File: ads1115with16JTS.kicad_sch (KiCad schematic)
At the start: 52 parts, among them J1 Conn_01x02_Pin, J10 Conn_01x02_Pin, J11 Conn_01x02_Pin, J12 Conn_01x02_Pin, J13 Conn_01x02_Pin, J14 Conn_01x02_Pin, J15 Conn_01x02_Pin, J16 Conn_01x02_Pin, J17 Conn_01x04_Pin, J18 PinSocket_1x20_P2.54mm_Vertic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, J19 PinSocket_1x20_P2.54mm_Vertic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, J2 Conn_01x02_Pin, J20 Screw_Terminal_01x02, J3 Conn_01x02_Pin, J4 Conn_01x02_Pin, J5 Conn_01x02_Pin, J6 Conn_01x02_Pin, J7 Conn_01x02_Pin, J8 Conn_01x02_Pin, J9 Conn_01x02_Pin, U1 ADS1115IDGS, U2 ADS1115IDGS, U3 ADS1115IDGS, U4 ADS1115IDGS

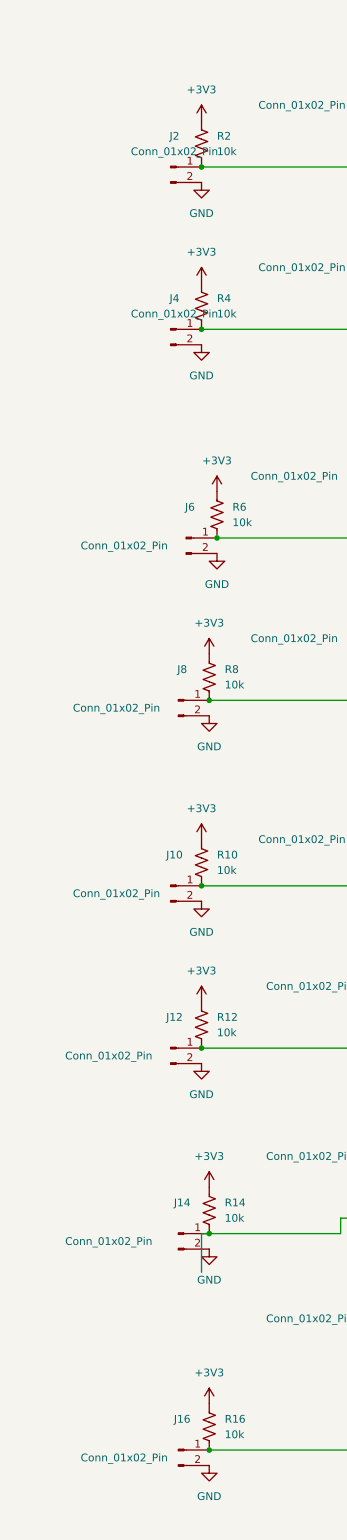
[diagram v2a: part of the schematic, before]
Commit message: sized slightly larger, added 2 more mounting holes.
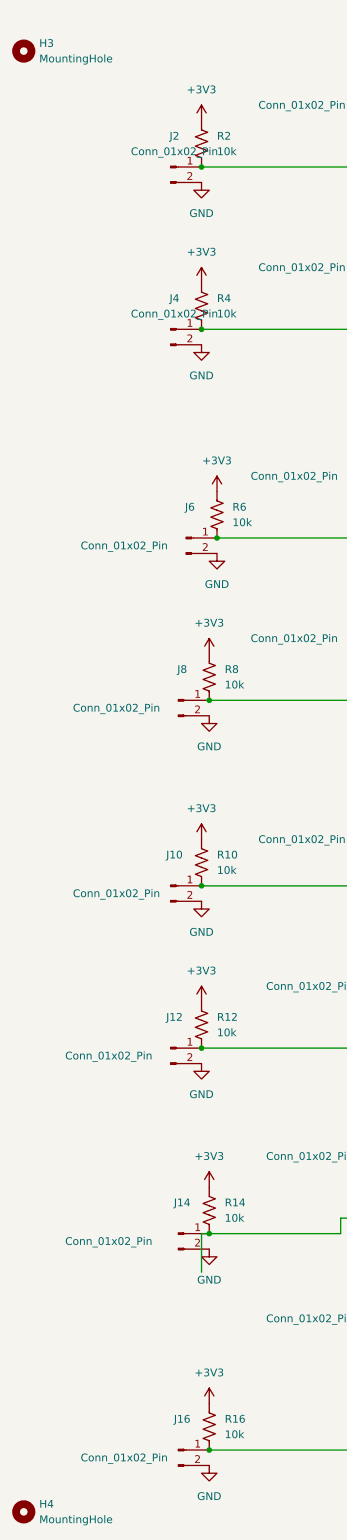
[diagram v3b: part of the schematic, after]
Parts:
- added H3, H4: MountingHole, MountingHole:MountingHole_2.2mm_M2_ISO7380_Pad, symbol ProjectLib:MountingHole
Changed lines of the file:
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@@
+    )
+  )
+  (symbol (lib_id "ProjectLib:MountingHole") (at 19.05 20.32 0) (unit 1)
+    (in_bom yes) (on_board yes) (dnp no) (fields_autoplaced)
+    (property "Reference" "H3" (at 21.59 19.05 0)
+      (effects (font (size 1.27 1.27)) (justify left))
+    )
+    (property "Value" "MountingHole" (at 21.59 21.59 0)
+      (effects (font (size 1.27 1.27)) (justify left))
+    )
+    (property "Footprint" "MountingHole:MountingHole_2.2mm_M2_ISO7380_Pad" (at 19.05 20.32 0)
+      (effects (font (size 1.27 1.27)) hide)
+    )
+    (property "Datasheet" "~" (at 19.05 20.32 0)
+      (effects (font (size 1.27 1.27)) hide)
+    )
+    (instances
+      (project "ads1115with16JTS"
+        (path "/0c2d0c14-8850-4a30-bb78-b2f40cb442ba"
+          (reference "H3") (unit 1)
+        )
+      )
     )
   )
@@
         )
       )
+    )
+  )
+  (symbol (lib_id "ProjectLib:MountingHole") (at 19.05 260.35 0) (unit 1)
+    (in_bom yes) (on_board yes) (dnp no) (fields_autoplaced)
+    (property "Reference" "H4" (at 21.59 259.08 0)
+      (effects (font (size 1.27 1.27)) (justify left))
+    )
+    (property "Value" "MountingHole" (at 21.59 261.62 0)
+      (effects (font (size 1.27 1.27)) (justify left))
+    )
+    (property "Footprint" "MountingHole:MountingHole_2.2mm_M2_ISO7380_Pad" (at 19.05 260.35 0)
+      (effects (font (size 1.27 1.27)) hide)
+    )
+    (property "Datasheet" "~" (at 19.05 260.35 0)
+      (effects (font (size 1.27 1.27)) hide)
+    )
+    (instances
+      (project "ads1115with16JTS"
+        (path "/0c2d0c14-8850-4a30-bb78-b2f40cb442ba"
+          (reference "H4") (unit 1)
+        )
+      )

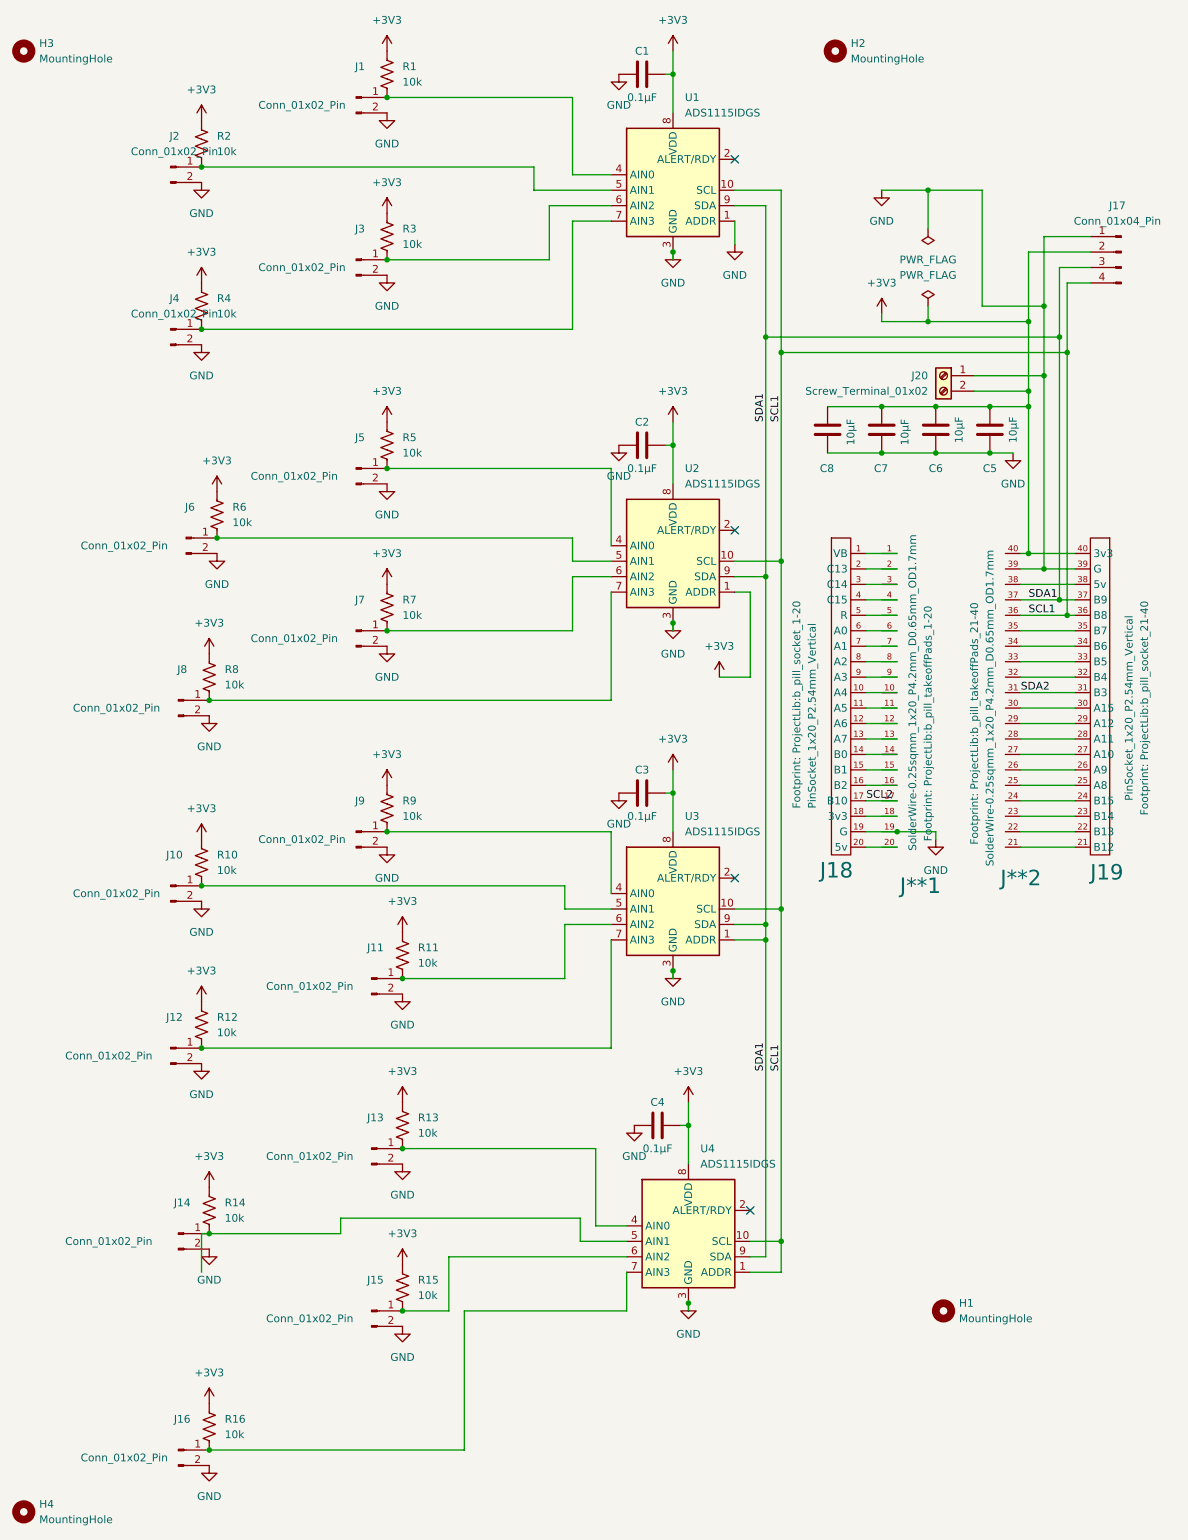
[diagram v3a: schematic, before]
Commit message: Footprint adjustments to get tthem all from ProjectLib.pretty. Using Kicad 8.0.1.
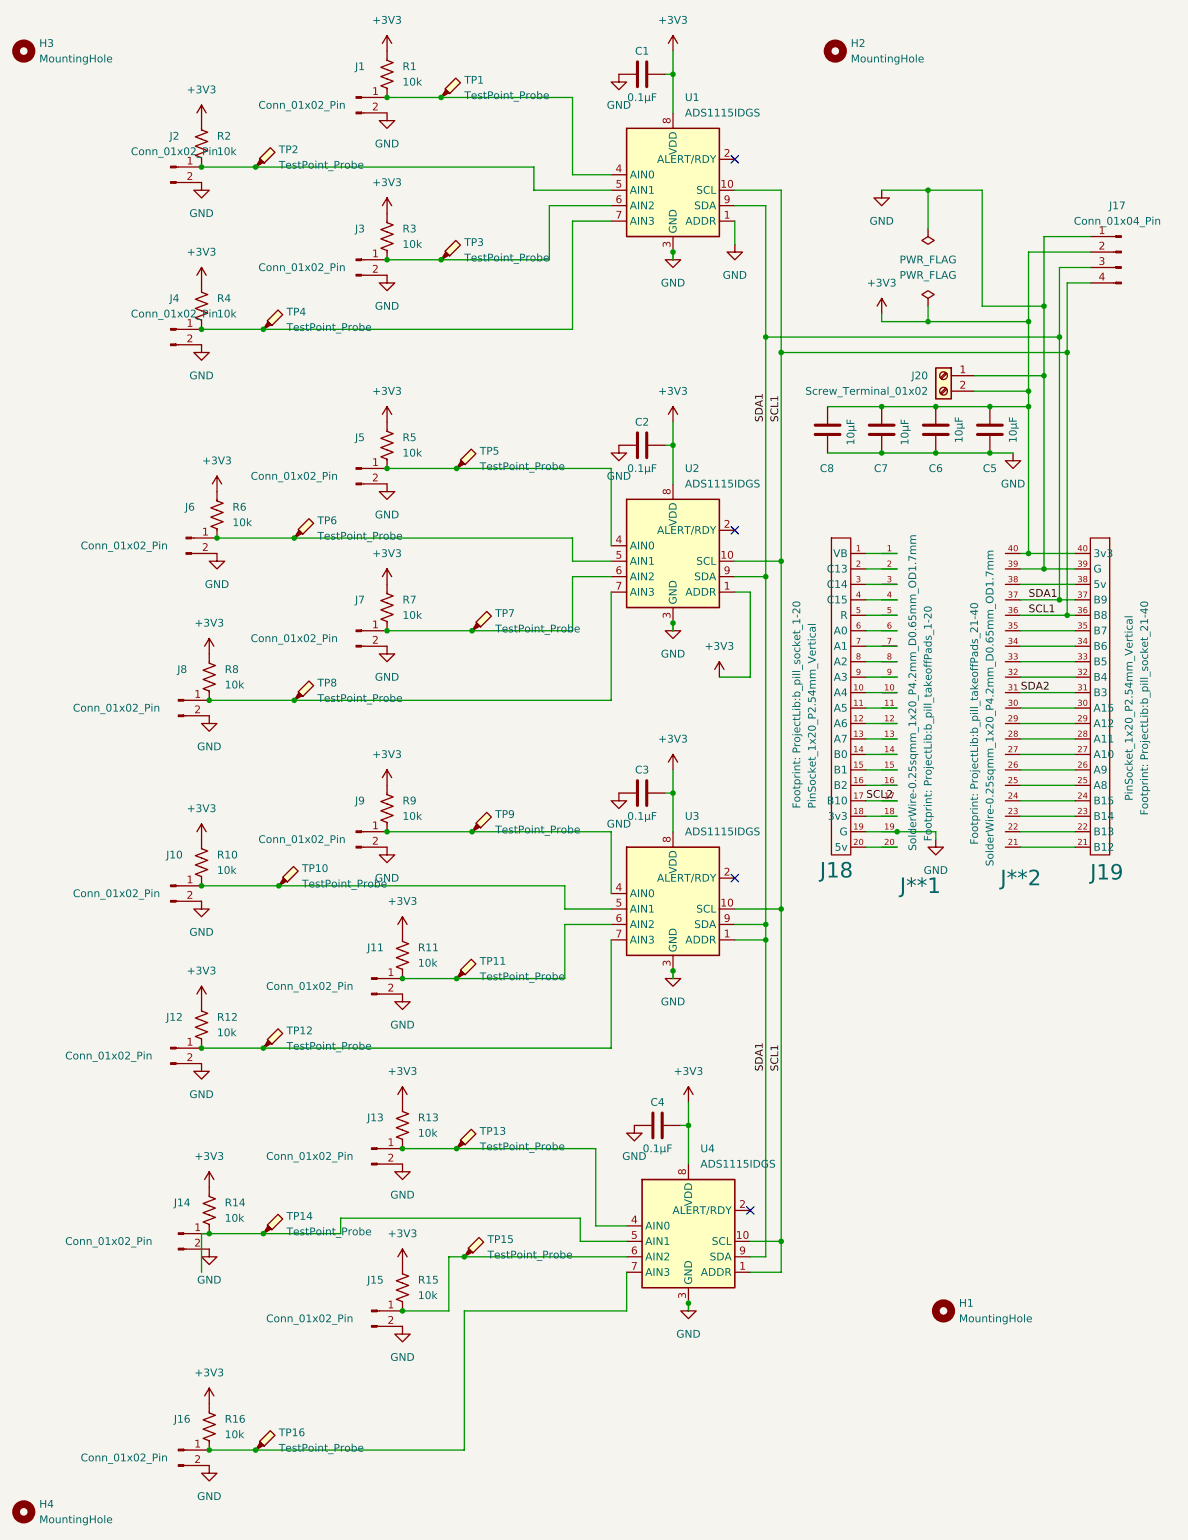
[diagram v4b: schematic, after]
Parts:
- added TP1, TP10, TP11, TP12, TP13, TP14, TP15, TP16, TP2, TP3, TP4, TP5, TP6, TP7, TP8, TP9: TestPoint_Probe, TestPoint:TestPoint_THTPad_D1.0mm_Drill0.5mm, symbol ProjectLib:TestPoint_Probe
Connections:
- net at J15.1 (Pin_1), R15.2, U4.6 (AIN2): now also TP15.1
- net at J1.1 (Pin_1), R1.2, U1.4 (AIN0): now also TP1.1
- net at J2.1 (Pin_1), R2.2, U1.5 (AIN1): now also TP2.1
- net at J3.1 (Pin_1), R3.2, U1.6 (AIN2): now also TP3.1
- net at J4.1 (Pin_1), R4.2, U1.7 (AIN3): now also TP4.1
- net at J16.1 (Pin_1), R16.2, U4.7 (AIN3): now also TP16.1
- net at J12.1 (Pin_1), R12.2, U3.7 (AIN3): now also TP12.1
- net at J11.1 (Pin_1), R11.2, U3.6 (AIN2): now also TP11.1
- net at J13.1 (Pin_1), R13.2, U4.4 (AIN0): now also TP13.1
- net at J14.1 (Pin_1), R14.2, U4.5 (AIN1): now also TP14.1
- net at J10.1 (Pin_1), R10.2, U3.5 (AIN1): now also TP10.1
- net at J8.1 (Pin_1), R8.2, U2.7 (AIN3): now also TP8.1
- net at J9.1 (Pin_1), R9.2, U3.4 (AIN0): now also TP9.1
- net at J7.1 (Pin_1), R7.2, U2.6 (AIN2): now also TP7.1
- net at J6.1 (Pin_1), R6.2, U2.5 (AIN1): now also TP6.1
- net at J5.1 (Pin_1), R5.2, U2.4 (AIN0): now also TP5.1

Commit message: Removed test points because there is no room. Trying to sync symbol footprints and pcb footprints.
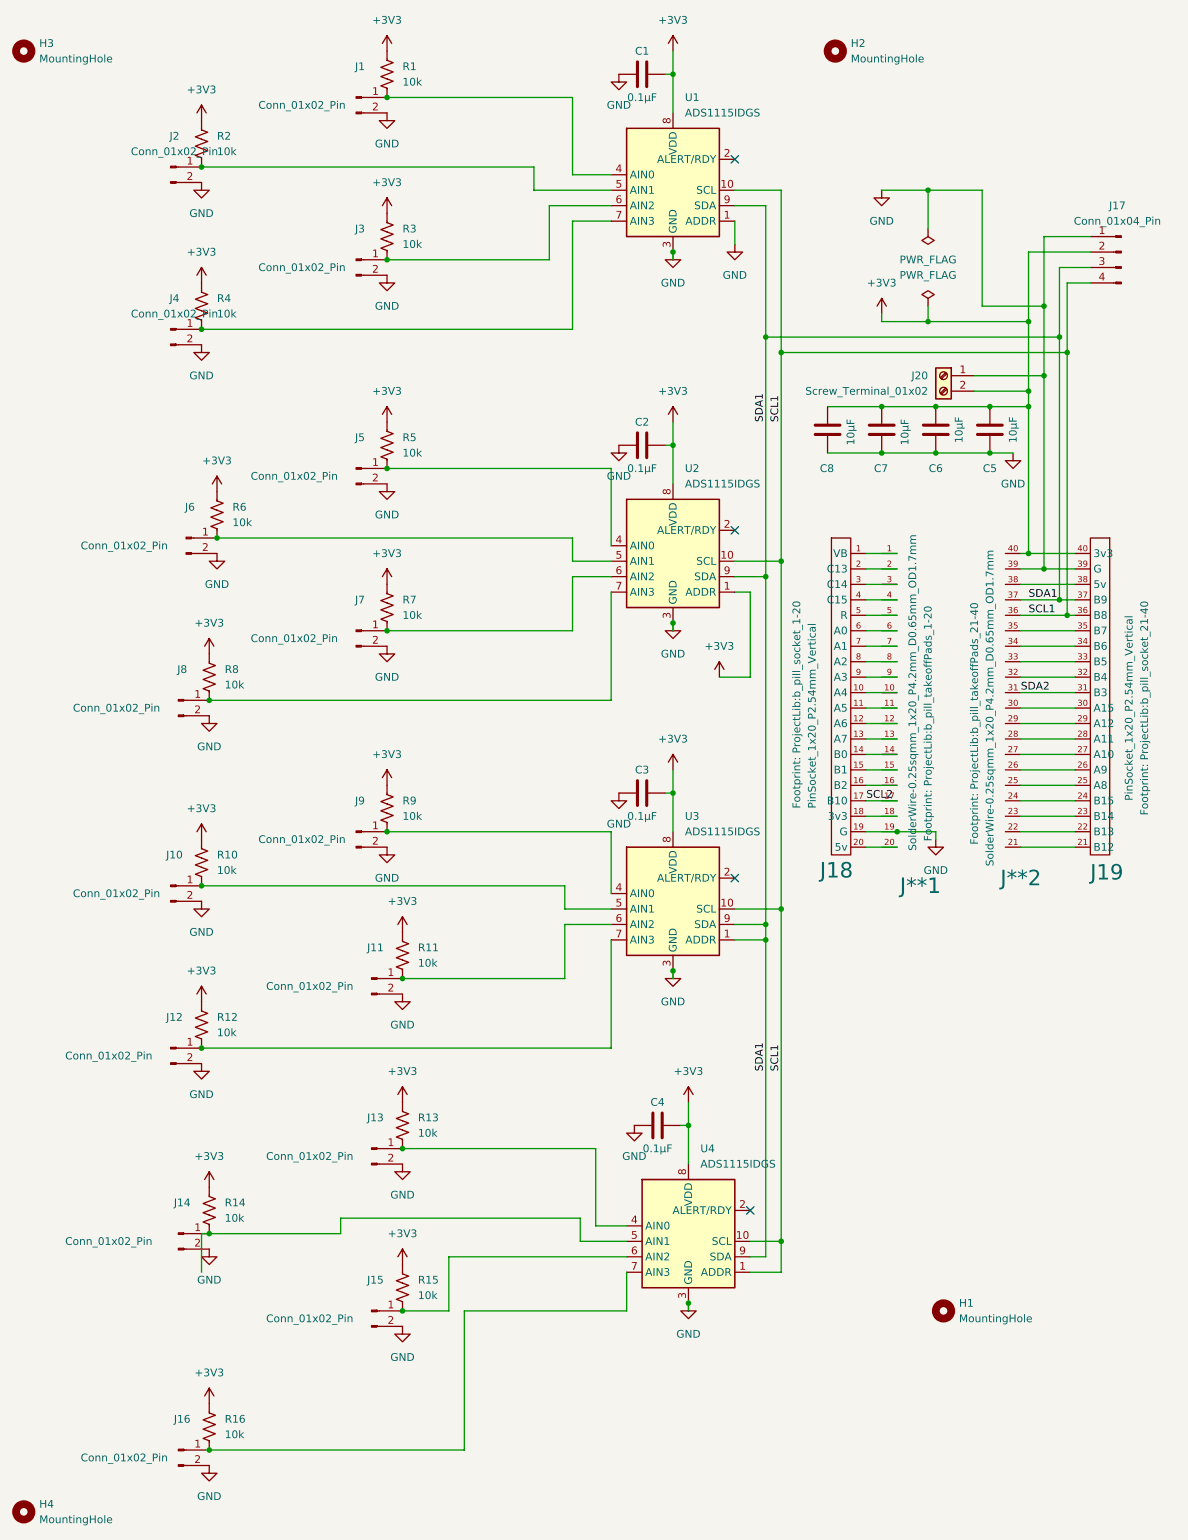
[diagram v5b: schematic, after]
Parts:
- removed TP1, TP10, TP11, TP12, TP13, TP14, TP15, TP16, TP2, TP3, TP4, TP5, TP6, TP7, TP8, TP9: TestPoint_Probe, TestPoint:TestPoint_THTPad_D1.0mm_Drill0.5mm, symbol ProjectLib:TestPoint_Probe
- H1, H2, H3, H4: footprint MountingHole:MountingHole_2.2mm_M2_ISO7380_Pad -> ProjectLib:MountingHole_2.2mm_M2_ISO7380_Pad

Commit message: DRC runs clean.
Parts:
- removed C7, C8: 10µF, ProjectLib:C_0805_2012Metric, symbol Device:C
- added C7, C8: 10µF, ProjectLib:C_0805_2012Metric, symbol ProjectLib:C
- C1, C2, C3, C4, C5, C6: footprint Capacitor_SMD:C_0805_2012Metric -> ProjectLib:C_0805_2012Metric
- J1, J10, J11, J12, J13, J14, J15, J16, J2, J3, J4, J5, J6, J7, J8, J9: footprint Connector_JST:JST_XH_B2B-XH-A_1x02_P2.50mm_Vertical -> ProjectLib:JST_XH_B2B-XH-A_1x02_P2.50mm_Vertical
- J20: footprint TerminalBlock_Phoenix:TerminalBlock_Phoenix_MPT-0,5-2-2.54_1x02_P2.54mm_Horizontal -> ProjectLib:TerminalBlock_Phoenix_MPT-0,5-2-2.54_1x02_P2.54mm_Horizontal
- R1, R10, R11, R12, R13, R14, R15, R16, R2, R3, R4, R5, R6, R7, R8, R9: footprint Resistor_SMD:R_0603_1608Metric -> ProjectLib:R_0603_1608Metric
- U1, U2, U3, U4: footprint Package_SO:TSSOP-10_3x3mm_P0.5mm -> ProjectLib:TSSOP-10_3x3mm_P0.5mm
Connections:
- net +3V3: now also C7.1, C8.1
- net GND: now also C7.2, C8.2

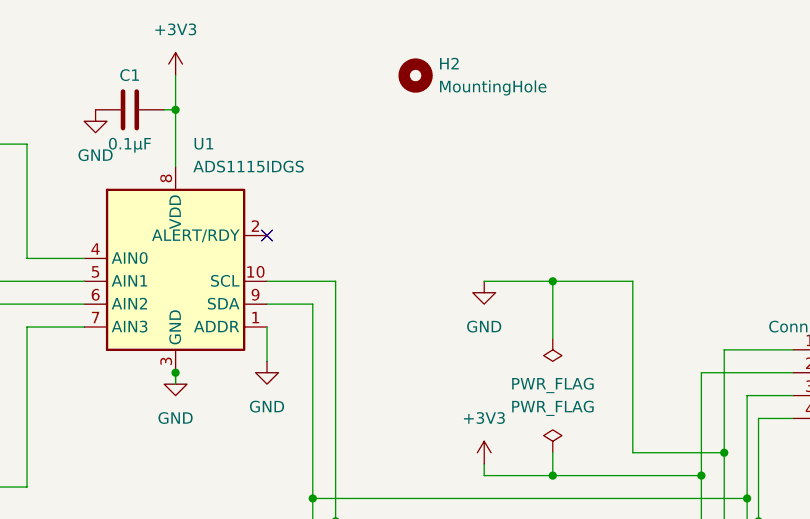
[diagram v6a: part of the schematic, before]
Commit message: added pullup on scl, sda. Other ongoing minor adjustments.
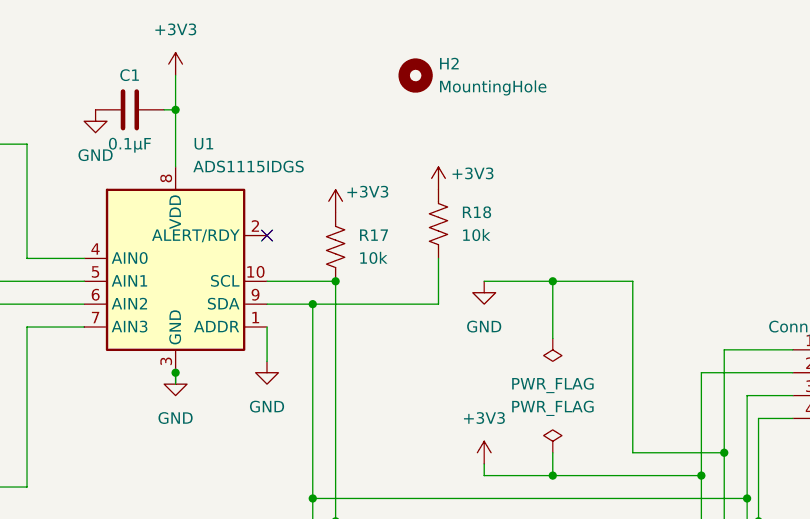
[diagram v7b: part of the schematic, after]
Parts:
- added R17, R18: 10k, ProjectLib:R_0603_1608Metric, symbol ProjectLib:R_US
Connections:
- net +3V3: now also R17.1, R18.1
- net SCL1: now also R17.2
- net SDA1: now also R18.2
